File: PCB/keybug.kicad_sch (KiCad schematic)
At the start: 8 parts, among them U2 rp2040-zero

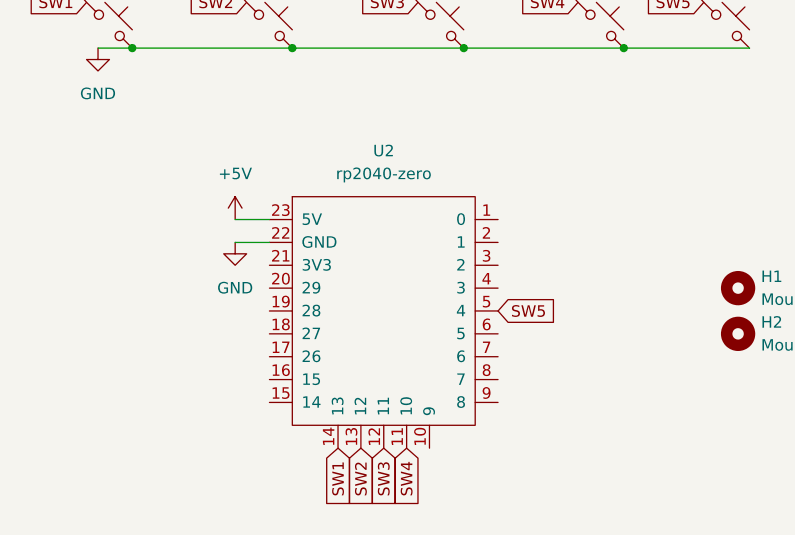
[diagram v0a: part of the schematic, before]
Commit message: PCB+Firmware: make board reversible
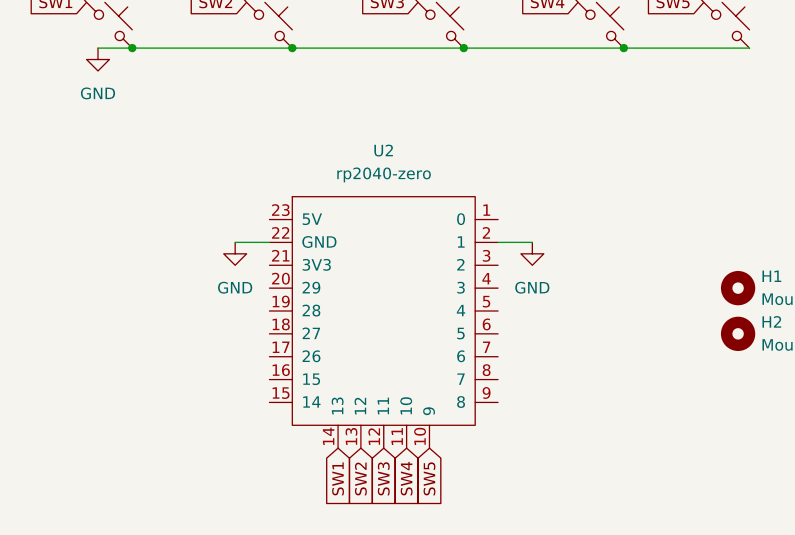
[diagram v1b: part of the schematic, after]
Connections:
- net GND: now also U2.2 (1)
- net SW5: now also U2.10 (9); no longer U2.5 (4)
- net +5V: no longer names the net of U2.23 (5V)
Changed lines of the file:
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@@
 	(wire
 		(pts
-			(xy 74.93 60.96) (xy 78.74 60.96)
+			(xy 104.14 63.5) (xy 107.95 63.5)
 		)
 		(stroke
@@
 	(global_label "SW5"
 		(shape input)
-		(at 104.14 71.12 0)
+		(at 96.52 86.36 270)
 		(fields_autoplaced yes)
 		(effects
@@
 				(size 1.27 1.27)
 			)
-			(justify left)
+			(justify right)
 		)
 		(property "Intersheetrefs" "${INTERSHEET_REFS}"
-			(at 110.9956 71.12 0)
-			(effects
-				(font
-					(size 1.27 1.27)
-				)
-				(justify left)
+			(at 96.52 93.2156 90)
+			(effects
+				(font
+					(size 1.27 1.27)
+				)
+				(justify right)
 				(hide yes)
 			)
@@
 	)
 	(symbol
-		(lib_id "power:+5V")
-		(at 74.93 60.96 0)
-		(unit 1)
-		(exclude_from_sim no)
-		(in_bom yes)
-		(on_board yes)
-		(dnp no)
-		(fields_autoplaced yes)
-		(property "Reference" "#PWR016"
-			(at 74.93 64.77 0)
-			(effects
-				(font
-					(size 1.27 1.27)
-				)
-				(hide yes)
-			)
-		)
-		(property "Value" "+5V"
-			(at 74.93 55.88 0)
-			(effects
-				(font
-					(size 1.27 1.27)
-				)
-			)
-		)
-		(property "Footprint" ""
-			(at 74.93 60.96 0)
-			(effects
-				(font
-					(size 1.27 1.27)
-				)
-				(hide yes)
-			)
-		)
-		(property "Datasheet" ""
-			(at 74.93 60.96 0)
-			(effects
-				(font
-					(size 1.27 1.27)
-				)
-				(hide yes)
-			)
-		)
-		(property "Description" "Power symbol creates a global label with name \"+5V\""
-			(at 74.93 60.96 0)
-			(effects
-				(font
-					(size 1.27 1.27)
-				)
-				(hide yes)
-			)
-		)
-		(pin "1"
-		)
-		(instances
-			(project "debugKeyboard"
-				(path "/caab6239-5d38-4680-9968-5e16c34d2ebe"
-					(reference "#PWR016")
-					(unit 1)
-				)
-			)
-		)
-	)
-	(symbol
 		(lib_id "PCM_marbastlib-mx:MX_SW_solder")
 		(at 78.74 39.37 0)
@@
 					(unit 1)
 				)
+			)
+		)
+	)
+	(symbol
+		(lib_id "power:GND")
+		(at 107.95 63.5 0)
+		(unit 1)
+		(exclude_from_sim no)
+		(in_bom yes)
+		(on_board yes)
+		(dnp no)
+		(fields_autoplaced yes)
+		(property "Reference" "#PWR01"
+			(at 107.95 69.85 0)
+			(effects
+				(font
+					(size 1.27 1.27)
+				)
+				(hide yes)
+			)
+		)
+		(property "Value" "GND"
+			(at 107.95 68.58 0)
+			(effects
+				(font
+					(size 1.27 1.27)
+				)
+			)
+		)
+		(property "Footprint" ""
+			(at 107.95 63.5 0)
+			(effects
+				(font
+					(size 1.27 1.27)
+				)
+				(hide yes)
+			)
+		)
+		(property "Datasheet" ""
+			(at 107.95 63.5 0)
+			(effects
+				(font
+					(size 1.27 1.27)
+				)
+				(hide yes)
+			)
+		)
+		(property "Description" "Power symbol creates a global label with name \"GND\" , ground"
+			(at 107.95 63.5 0)
+			(effects
+				(font
+					(size 1.27 1.27)
+				)
+				(hide yes)
+			)
+		)
+		(pin "1"
+		)
+		(instances
+			(project "keybug"
+				(path "/caab6239-5d38-4680-9968-5e16c34d2ebe"
+					(reference "#PWR01")
+					(unit 1)
+				)

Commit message: Add LEDs to PCB
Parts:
- added LED1, LED2, LED3, LED4, LED5: MX_SK6812MINI-E, PCM_marbastlib-mx:LED_MX_6028R-ROT, symbol PCM_marbastlib-mx:MX_SK6812MINI-E
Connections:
- net GND: now also LED1.4 (VSS), LED2.4 (VSS), LED3.4 (VSS), LED4.4 (VSS), LED5.4 (VSS)
- net VDD: now reaches U2.1 (0)
- net VDD: now also U2.23 (5V), LED1.1 (VDD), LED2.1 (VDD), LED3.1 (VDD), LED4.1 (VDD), LED5.1 (VDD)
- net RGB: now reaches U2.15 (14)
- net RGB: now also U2.9 (8), LED5.3 (DIN)
- new net: LED1.3 (DIN), LED2.2 (DOUT)
- new net: LED2.3 (DIN), LED3.2 (DOUT)
- new net: LED4.3 (DIN), LED5.2 (DOUT)
- new net: LED3.3 (DIN), LED4.2 (DOUT)
- no-connect marks 0 -> 1
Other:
- moved on the sheet: H1, H2, MX1, MX2, MX3, MX4, MX5, U2
